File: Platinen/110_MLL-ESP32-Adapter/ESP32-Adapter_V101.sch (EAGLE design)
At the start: 90 parts, among them IC1 ISO1050, J1.7 JUMPER-SMT_2_NO_SILK, J2.2 JUMPER-SMT_2_NO_SILK, J2.3 JUMPER-SMT_2_NO_SILK, J2.4 JUMPER-SMT_2_NO_SILK, J2.5 JUMPER-SMT_2_NO_SILK, J2.6 JUMPER-SMT_2_NO_SILK, J2.7 JUMPER-SMT_2_NO_SILK, J3.2 JUMPER-SMT_2_NO_SILK, J3.3 JUMPER-SMT_2_NO_SILK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

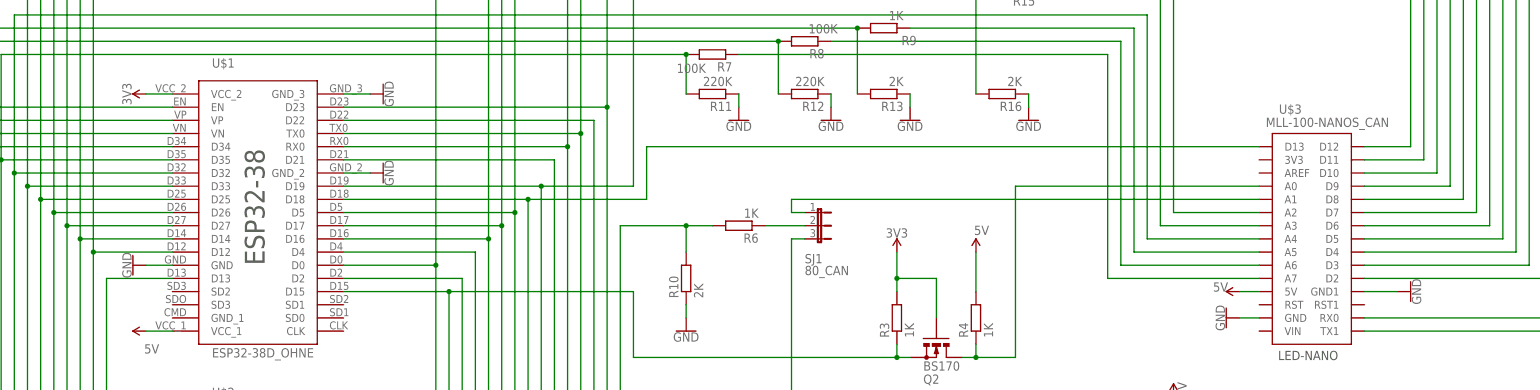
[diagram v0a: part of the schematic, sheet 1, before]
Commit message: Update 110_MLL-ESP32-Adapter
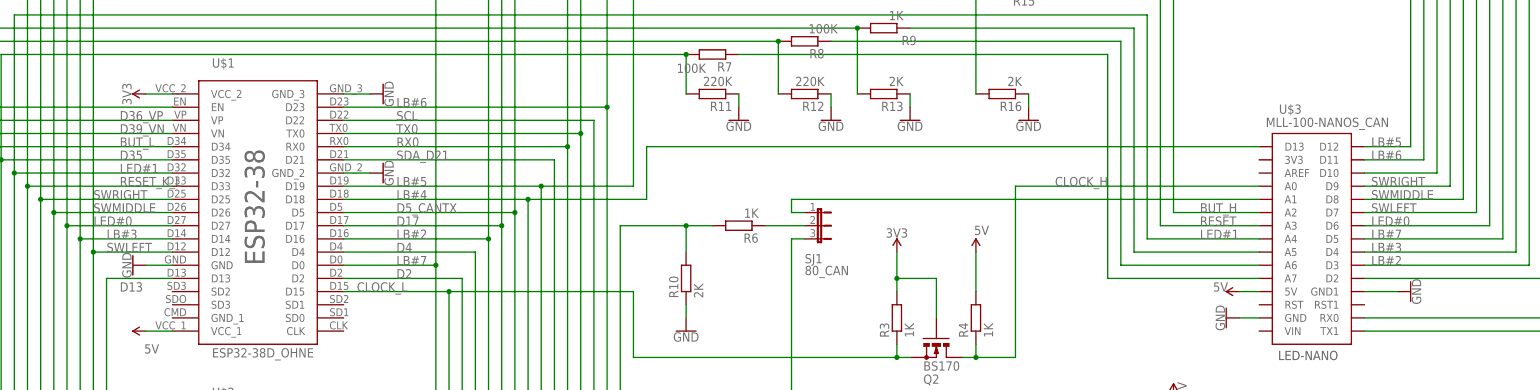
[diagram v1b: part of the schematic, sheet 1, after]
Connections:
- net A2_HV renamed BUT_H
- net D12 renamed SWLEFT
- net D15 renamed CLOCK_L
- net D26 renamed SWMIDDLE
- net D27 renamed LED#0
- net D32 renamed LED#1
- net D33 renamed RESET_K_L
- net D34 renamed BUT_L
- net N$22 renamed RESET
- net N$3 renamed SWRIGHT
- net N$4 renamed CLOCK_H
